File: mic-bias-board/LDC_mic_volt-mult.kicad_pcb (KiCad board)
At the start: 2 copper layers, 38 x 52 mm, 32 parts, among them U1 HCF40106_Hex-Inverter

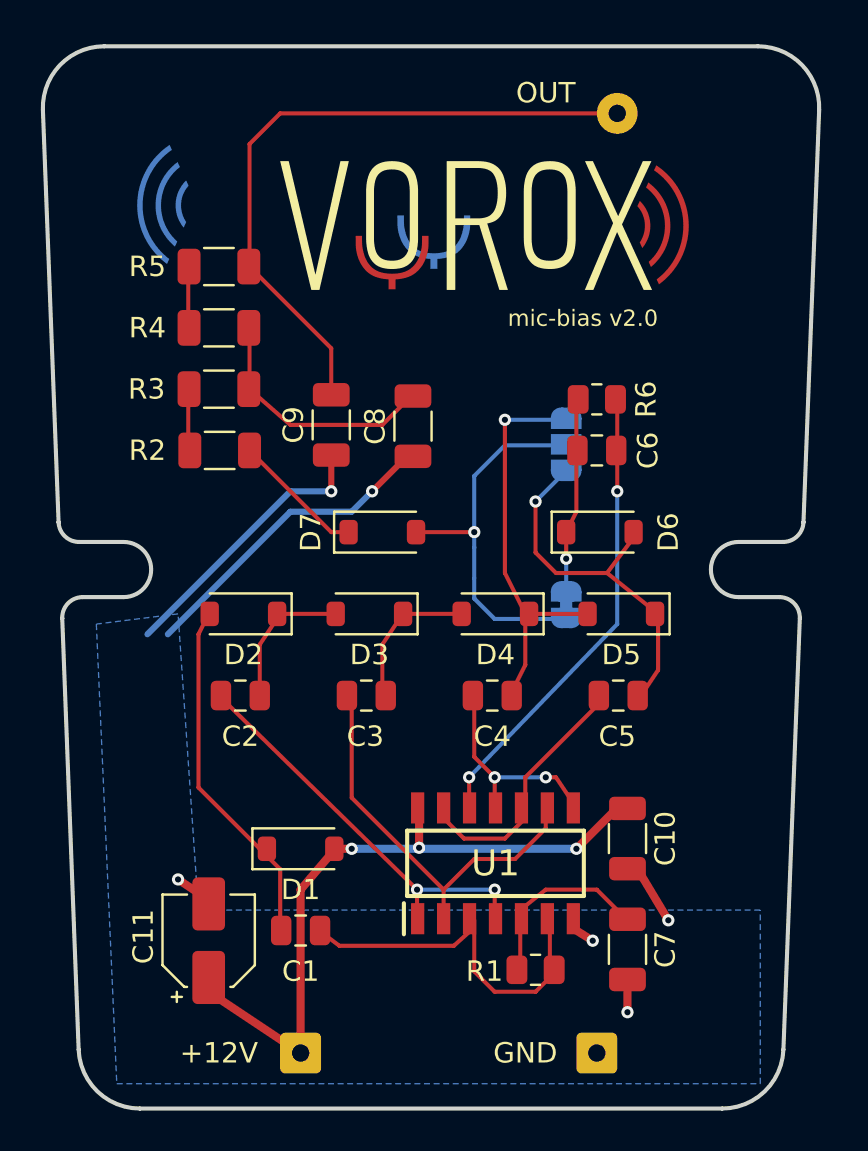
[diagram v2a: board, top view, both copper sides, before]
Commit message: input/output connectors moved to 2.54mm spacing. Improved clearance around screw slots.
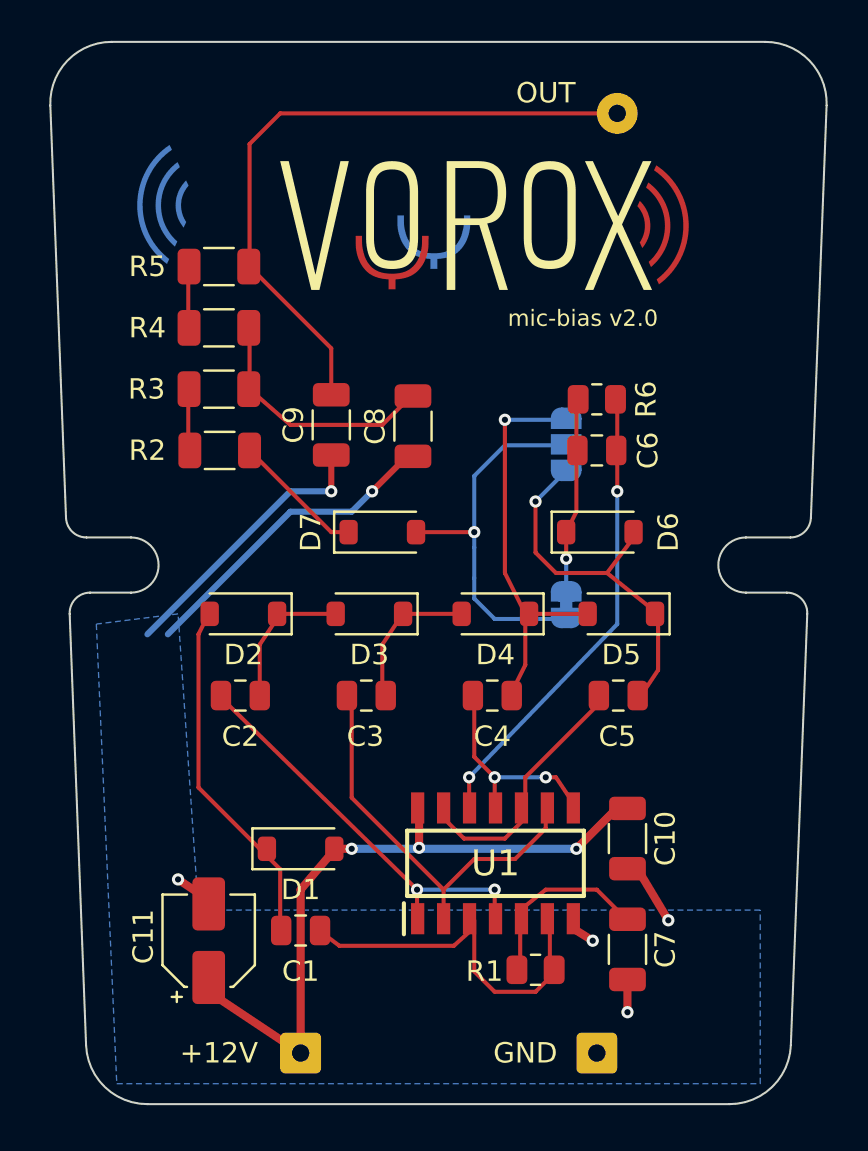
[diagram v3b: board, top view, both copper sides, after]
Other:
- outline, holes or cut-outs redrawn
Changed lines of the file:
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@@
 		(net 21)
 	)
-	(gr_arc
-		(start 80.937907 59.679993)
-		(mid 81.658329 59.986457)
-		(end 81.937184 60.718009)
-		(stroke
-			(width 0.2)
-			(type default)
-		)
-		(layer "Edge.Cuts")
-	)
-	(gr_line
-		(start 48.834011 56.979993)
-		(end 46.651311 56.979993)
-		(stroke
-			(width 0.2)
-			(type default)
-		)
-		(layer "Edge.Cuts")
-	)
-	(gr_arc
-		(start 49.631843 84.715945)
-		(mid 47.551235 83.877211)
-		(end 46.634011 81.829991)
-		(stroke
-			(width 0.2)
-			(type default)
-		)
-		(layer "Edge.Cuts")
-	)
-	(gr_arc
-		(start 81.134011 81.829992)
-		(mid 80.216787 83.877211)
-		(end 78.136178 84.715945)
-		(stroke
-			(width 0.2)
-			(type default)
-		)
-		(layer "Edge.Cuts")
-	)
-	(gr_line
-		(start 48.834011 59.679993)
-		(end 46.830114 59.679993)
-		(stroke
-			(width 0.2)
-			(type default)
-		)
-		(layer "Edge.Cuts")
-	)
-	(gr_line
-		(start 78.934011 59.679993)
-		(end 80.937907 59.679993)
-		(stroke
-			(width 0.2)
-			(type default)
-		)
-		(layer "Edge.Cuts")
-	)
-	(gr_arc
-		(start 44.884011 35.829991)
-		(mid 45.720575 33.635337)
-		(end 47.881841 32.715945)
-		(stroke
-			(width 0.2)
-			(type default)
-		)
-		(layer "Edge.Cuts")
-	)
-	(gr_line
-		(start 45.652033 56.018009)
-		(end 44.884011 35.829991)
-		(stroke
-			(width 0.2)
-			(type default)
-		)
-		(layer "Edge.Cuts")
-	)
-	(gr_arc
-		(start 45.830839 60.718009)
-		(mid 46.109693 59.986457)
-		(end 46.830114 59.679993)
-		(stroke
-			(width 0.2)
-			(type default)
-		)
-		(layer "Edge.Cuts")
-	)
-	(gr_line
-		(start 45.652034 56.018009)
-		(end 45.652033 56.018009)
-		(stroke
-			(width 0.2)
-			(type default)
-		)
-		(layer "Edge.Cuts")
-	)
-	(gr_arc
-		(start 79.886181 32.715945)
-		(mid 82.047446 33.635337)
-		(end 82.884011 35.829991)
-		(stroke
-			(width 0.2)
-			(type default)
-		)
-		(layer "Edge.Cuts")
-	)
-	(gr_arc
-		(start 46.651311 56.979993)
-		(mid 45.957775 56.700415)
-		(end 45.652034 56.018009)
-		(stroke
-			(width 0.2)
-			(type default)
-		)
-		(layer "Edge.Cuts")
-	)
-	(gr_arc
-		(start 78.934011 59.679993)
-		(mid 77.584011 58.329993)
-		(end 78.934011 56.979993)
-		(stroke
-			(width 0.2)
-			(type default)
-		)
-		(layer "Edge.Cuts")
-	)
-	(gr_line
-		(start 78.934011 56.979993)
-		(end 81.116711 56.979993)
-		(stroke
-			(width 0.2)
-			(type default)
-		)
-		(layer "Edge.Cuts")
-	)
-	(gr_line
-		(start 49.631843 84.715945)
-		(end 78.136178 84.715945)
-		(stroke
-			(width 0.2)
-			(type default)
-		)
-		(layer "Edge.Cuts")
-	)
-	(gr_arc
-		(start 48.834011 56.979993)
-		(mid 50.184011 58.33)
-		(end 48.834011 59.679993)
-		(stroke
-			(width 0.2)
-			(type default)
-		)
-		(layer "Edge.Cuts")
-	)
-	(gr_line
-		(start 81.134011 81.829992)
-		(end 81.937184 60.718009)
-		(stroke
-			(width 0.2)
-			(type default)
-		)
-		(layer "Edge.Cuts")
-	)
-	(gr_line
-		(start 45.830839 60.718009)
-		(end 45.830838 60.718009)
-		(stroke
-			(width 0.2)
-			(type default)
-		)
-		(layer "Edge.Cuts")
-	)
-	(gr_line
-		(start 47.881841 32.715945)
-		(end 79.886181 32.715945)
-		(stroke
-			(width 0.2)
-			(type default)
-		)
-		(layer "Edge.Cuts")
-	)
-	(gr_line
-		(start 82.115988 56.018009)
-		(end 82.115989 56.018009)
-		(stroke
-			(width 0.2)
-			(type default)
-		)
-		(layer "Edge.Cuts")
-	)
-	(gr_line
-		(start 82.115989 56.018009)
-		(end 82.884011 35.829991)
-		(stroke
-			(width 0.2)
-			(type default)
-		)
-		(layer "Edge.Cuts")
-	)
-	(gr_line
-		(start 46.634011 81.829991)
-		(end 45.830838 60.718009)
-		(stroke
-			(width 0.2)
-			(type default)
-		)
-		(layer "Edge.Cuts")
-	)
-	(gr_arc
-		(start 82.115988 56.018009)
-		(mid 81.810248 56.700415)
-		(end 81.116711 56.979993)
-		(stroke
-			(width 0.2)
+	(gr_line
+		(start 82.479963 55.798016)
+		(end 83.247831 35.614048)
+		(stroke
+			(width 0.1)
+			(type default)
+		)
+		(layer "Edge.Cuts")
+	)
+	(gr_arc
+		(start 82.479963 55.798016)
+		(mid 82.174221 56.480421)
+		(end 81.480686 56.76)
+		(stroke
+			(width 0.1)
+			(type default)
+		)
+		(layer "Edge.Cuts")
+	)
+	(gr_arc
+		(start 49.995662 84.5)
+		(mid 47.915055 83.661266)
+		(end 46.997831 81.614048)
+		(stroke
+			(width 0.1)
+			(type default)
+		)
+		(layer "Edge.Cuts")
+	)
+	(gr_arc
+		(start 80.25 32.5)
+		(mid 82.411287 33.419382)
+		(end 83.247831 35.614048)
+		(stroke
+			(width 0.1)
+			(type default)
+		)
+		(layer "Edge.Cuts")
+	)
+	(gr_line
+		(start 49.197831 59.46)
+		(end 47.193781 59.46)
+		(stroke
+			(width 0.1)
+			(type default)
+		)
+		(layer "Edge.Cuts")
+	)
+	(gr_arc
+		(start 79.297831 59.46)
+		(mid 77.947831 58.11)
+		(end 79.297831 56.76)
+		(stroke
+			(width 0.1)
+			(type default)
+		)
+		(layer "Edge.Cuts")
+	)
+	(gr_arc
+		(start 49.197831 56.76)
+		(mid 50.547831 58.11)
+		(end 49.197831 59.46)
+		(stroke
+			(width 0.1)
+			(type default)
+		)
+		(layer "Edge.Cuts")
+	)
+	(gr_line
+		(start 81.497831 81.614048)
+		(end 82.301158 60.498016)
+		(stroke
+			(width 0.1)
+			(type default)
+		)
+		(layer "Edge.Cuts")
+	)
+	(gr_arc
+		(start 47.014976 56.76)
+		(mid 46.321443 56.48042)
+		(end 46.015699 55.798016)
+		(stroke
+			(width 0.1)
+			(type default)
+		)
+		(layer "Edge.Cuts")
+	)
+	(gr_line
+		(start 46.015699 55.798016)
+		(end 45.247831 35.614048)
+		(stroke
+			(width 0.1)
+			(type default)
+		)
+		(layer "Edge.Cuts")
+	)
+	(gr_line
+		(start 46.997831 81.614048)
+		(end 46.194504 60.498016)
+		(stroke
+			(width 0.1)
+			(type default)
+		)
+		(layer "Edge.Cuts")
+	)
+	(gr_line
+		(start 79.297831 56.76)
+		(end 81.480686 56.76)
+		(stroke
+			(width 0.1)
+			(type default)
+		)
+		(layer "Edge.Cuts")
+	)
+	(gr_arc
+		(start 46.194504 60.498016)
+		(mid 46.473359 59.766464)
+		(end 47.193781 59.46)
+		(stroke
+			(width 0.1)
+			(type default)
+		)
+		(layer "Edge.Cuts")
+	)
+	(gr_line
+		(start 49.995662 84.5)
+		(end 78.5 84.5)
+		(stroke
+			(width 0.1)
+			(type default)
+		)
+		(layer "Edge.Cuts")
+	)
+	(gr_line
+		(start 48.245662 32.5)
+		(end 80.25 32.5)
+		(stroke
+			(width 0.1)
+			(type default)
+		)
+		(layer "Edge.Cuts")
+	)
+	(gr_arc
+		(start 81.301881 59.46)
+		(mid 82.022303 59.766464)
+		(end 82.301158 60.498016)
+		(stroke
+			(width 0.1)
+			(type default)
+		)
+		(layer "Edge.Cuts")
+	)
+	(gr_arc
+		(start 81.497831 81.614048)
+		(mid 80.580607 83.661266)
+		(end 78.5 84.5)
+		(stroke
+			(width 0.1)
+			(type default)
+		)
+		(layer "Edge.Cuts")
+	)
+	(gr_line
+		(start 49.197831 56.76)
+		(end 47.014976 56.76)
+		(stroke
+			(width 0.1)
+			(type default)
+		)
+		(layer "Edge.Cuts")
+	)
+	(gr_line
+		(start 79.297831 59.46)
+		(end 81.301881 59.46)
+		(stroke
+			(width 0.1)
+			(type default)
+		)
+		(layer "Edge.Cuts")
+	)
+	(gr_arc
+		(start 45.247831 35.614048)
+		(mid 46.084396 33.419393)
+		(end 48.245662 32.5)
+		(stroke
+			(width 0.1)
 			(type default)
 		)
@@
 	)
 	(group ""
-		(members "0b06971a-383d-4535-86c7-48c0e00e54d4" "0cd6495e-dae4-428a-a55f-c7e0640f1555"
-			"2342d498-64dd-45cd-b407-677d08faf405" "2bcccb08-e86c-4fb8-bf73-e187078c23dd"
-			"3ea07625-7a8b-49a3-bf5d-83a0a7613406" "4cc09388-2d5c-45b5-87cc-9f972df82d2f"
-			"53714d87-abea-4d6d-9446-d9372924b264" "56a4b788-48e7-4f4b-bba4-674c8fb53216"
-			"56e34b65-d26a-439c-8679-4b45e036c889" "58ffea8e-bd11-4d37-b07d-71a50e90eb7a"
-			"6029384b-4a31-4144-8a15-a93a2af5f438" "68bdd9b5-82e4-4329-9d5b-70edb14d6bc3"
-			"7aad07fd-85cc-4891-8ae5-d487a1cef174" "8bf1fec1-f15b-4ddb-8d73-63b6ced05d4a"
-			"95d743db-4a0b-4d64-8bdf-3130f8956fde" "9a6bf93e-19b1-49ff-9e63-96b3f777903d"
-			"aa9a7a01-c6fb-4ed0-aa54-13efec545f5c" "bf623b41-f12c-486d-9007-4ded9c597831"
-			"c8de2b30-94cd-4dac-9102-b119ffd871cc" "cb28efe6-e7f6-4ee0-90f6-ae2a539022ef"
-			"d865a165-9261-42ad-9353-a397ed3362a0" "dbbaccc7-0f0e-41f7-819c-3a785e2e9dce"
-			"feb67cb3-f310-4678-a137-0e03555bca17"
-		)
+		(members "0e7cfd76-f1d4-462e-ab89-8c98d8ec5985" "157fd8b3-42ef-4f50-ab29-add7edea145b"
+			"2089635b-fd71-44ae-ae2e-5f67e507b526" "26ee7539-1d58-4989-accf-9d5ccc529542"
+			"342555f3-13f5-4d2b-8d72-5a8ddec67762" "3a21f60f-9177-4079-a01b-57d72b9e7598"
+			"3bc996d2-eb92-4dad-a86f-3822d723f7fa" "40c98a7a-46e9-4f7c-9e1e-5d6230d6dcf2"
+			"74ce200f-fab4-4f89-97bc-05829ba4b64c" "81cdc489-0f4f-4c85-a206-88358d5f8c34"
+			"95c8aeb4-b98c-4780-8d87-0da3f62b1bbe" "a52fb196-6277-4c7e-afd3-ef8c0b1546ac"
+			"b9ee27dc-62d3-44e1-aa9c-6523a554f766" "bc541285-aeb4-4f27-97c9-a84e9175b86a"
+			"c3c77d09-6849-444b-9491-9e6861e350d2" "dc6affec-b4da-45b7-b7c6-a6240765e34f"
+			"e26b9ca4-afa0-446b-b1fd-256cf64e2b59" "e9c04bb9-3131-4792-8b2f-dff205e61184"
+			"eb0404ed-0c20-4f47-8c87-cda380d8346e" "fa020659-44a8-4090-a71b-74593e11f7e2"
+		)
+	)
+	(group ""
+		(members "36978b16-88ec-4957-ab1e-a07193479e41")
 	)
 	(embedded_fonts no)
